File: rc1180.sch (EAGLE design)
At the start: 10 parts, among them IC1 LD117AS33TR

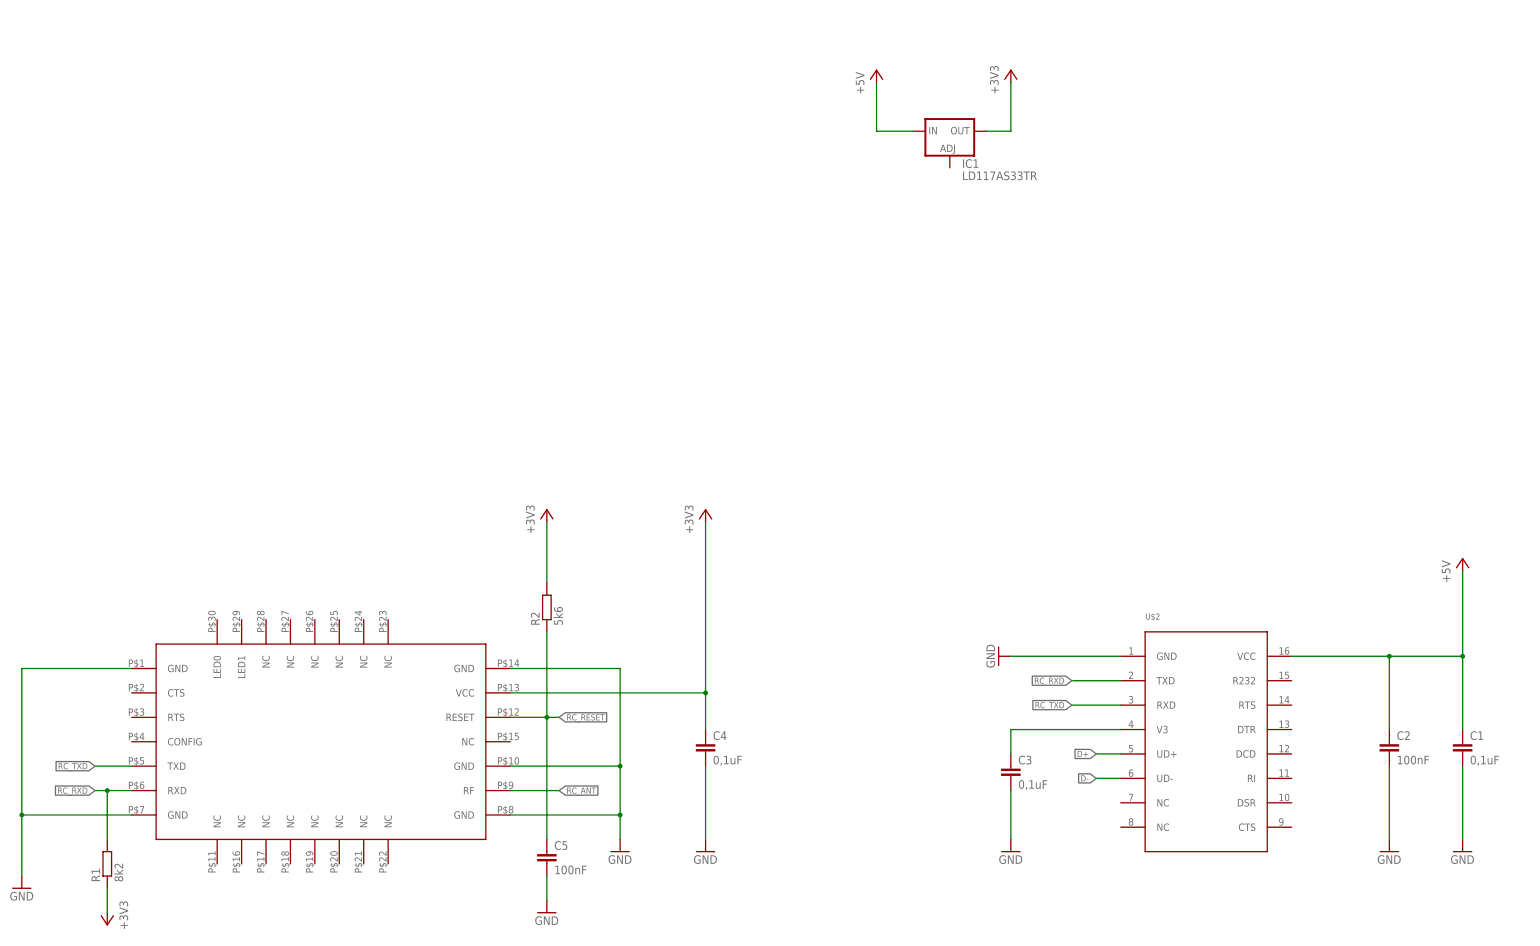
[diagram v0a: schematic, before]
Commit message: Added ch340 and ams1117 vreg
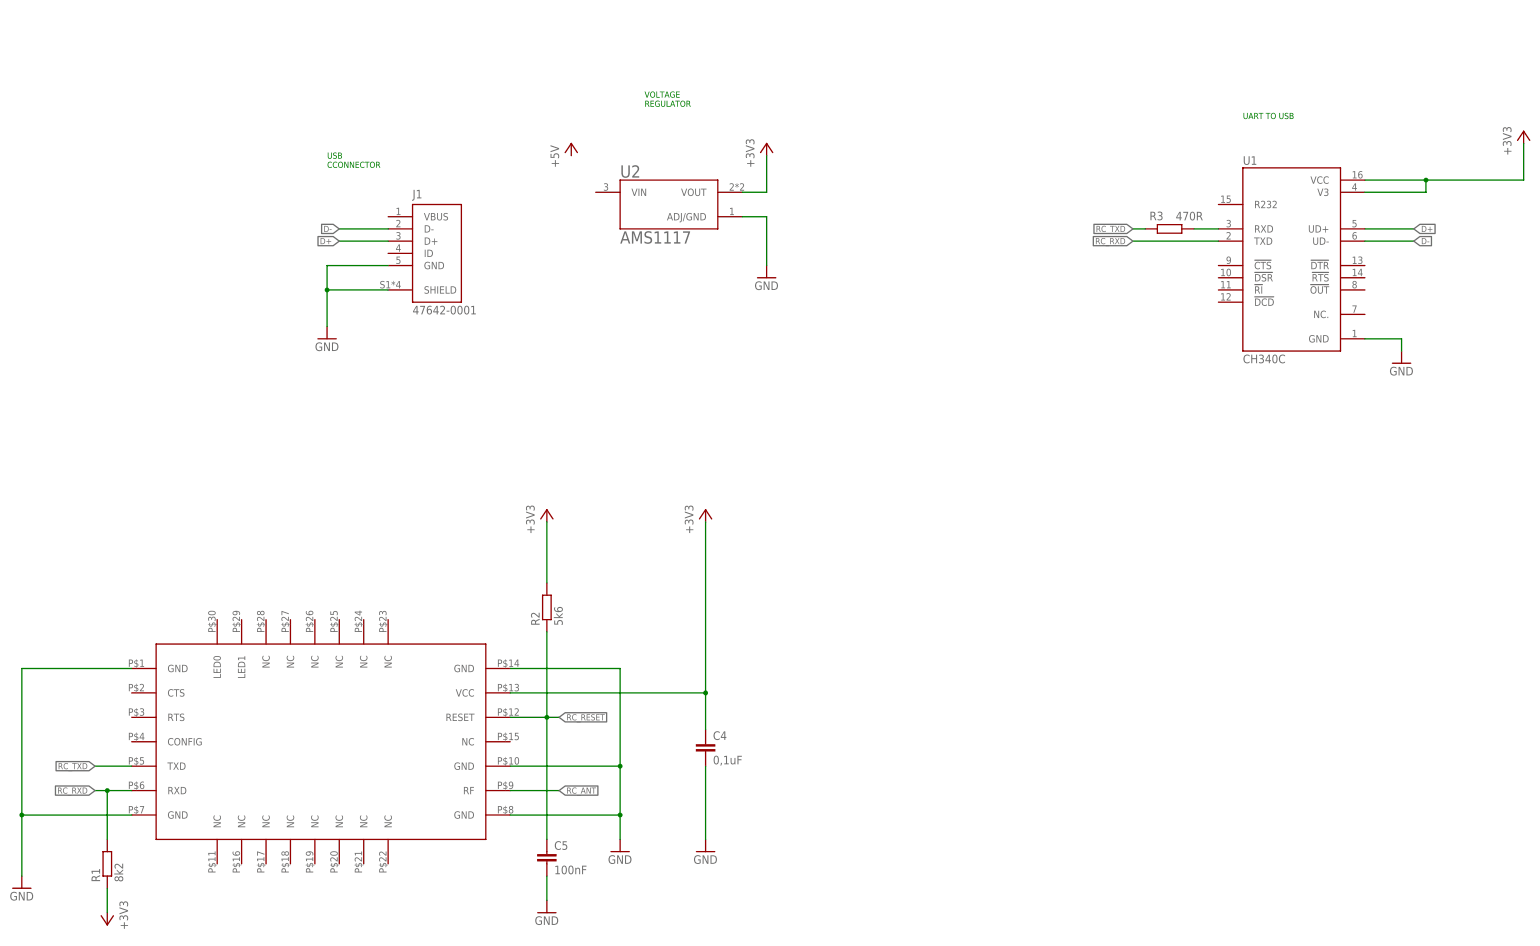
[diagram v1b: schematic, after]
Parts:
- removed C1, C3: 0,1uF, rcl:C-EUC1206K
- removed C2: 100nF, rcl:C-EUC0805
- removed IC1: LD117AS33TR, v-reg:LD117AS33TR
- removed U$2: CH340C, jacek27:CH340C
- added J1: 47642-0001, 47642-0001:47642-0001
- added R3: 470R, rcl:R-EU_R0805
- added U1: CH340C, CH340C:CH340C
- added U2: AMS1117, AMS1117:AMS1117
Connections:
- removed net +5V: C1.1, C2.1, IC1.IN, U$2.VCC
- net +3V3: now also U1.V3, U1.VCC, U2.VOUT; no longer IC1.OUT
- net D+: now also J1.D+, U1.UD+; no longer U$2.UD+
- net D-: now also J1.D-, U1.UD-; no longer U$2.UD-
- net GND: now also J1.GND, J1.SHIELD, U1.GND, U2.ADJ/GND; no longer C1.2, C2.2, C3.2, U$2.GND
- net N$1: now also R3.2, U1.RXD; no longer C3.1, U$2.V3
- net RC_RXD: now also U1.TXD; no longer U$2.TXD
- net RC_TXD: now also R3.1; no longer U$2.RXD
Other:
- note added: "UART TO USB"
- note added: "USB CCONNECTOR"
- note added: "VOLTAGE REGULATOR"

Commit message: Component placed / frame added
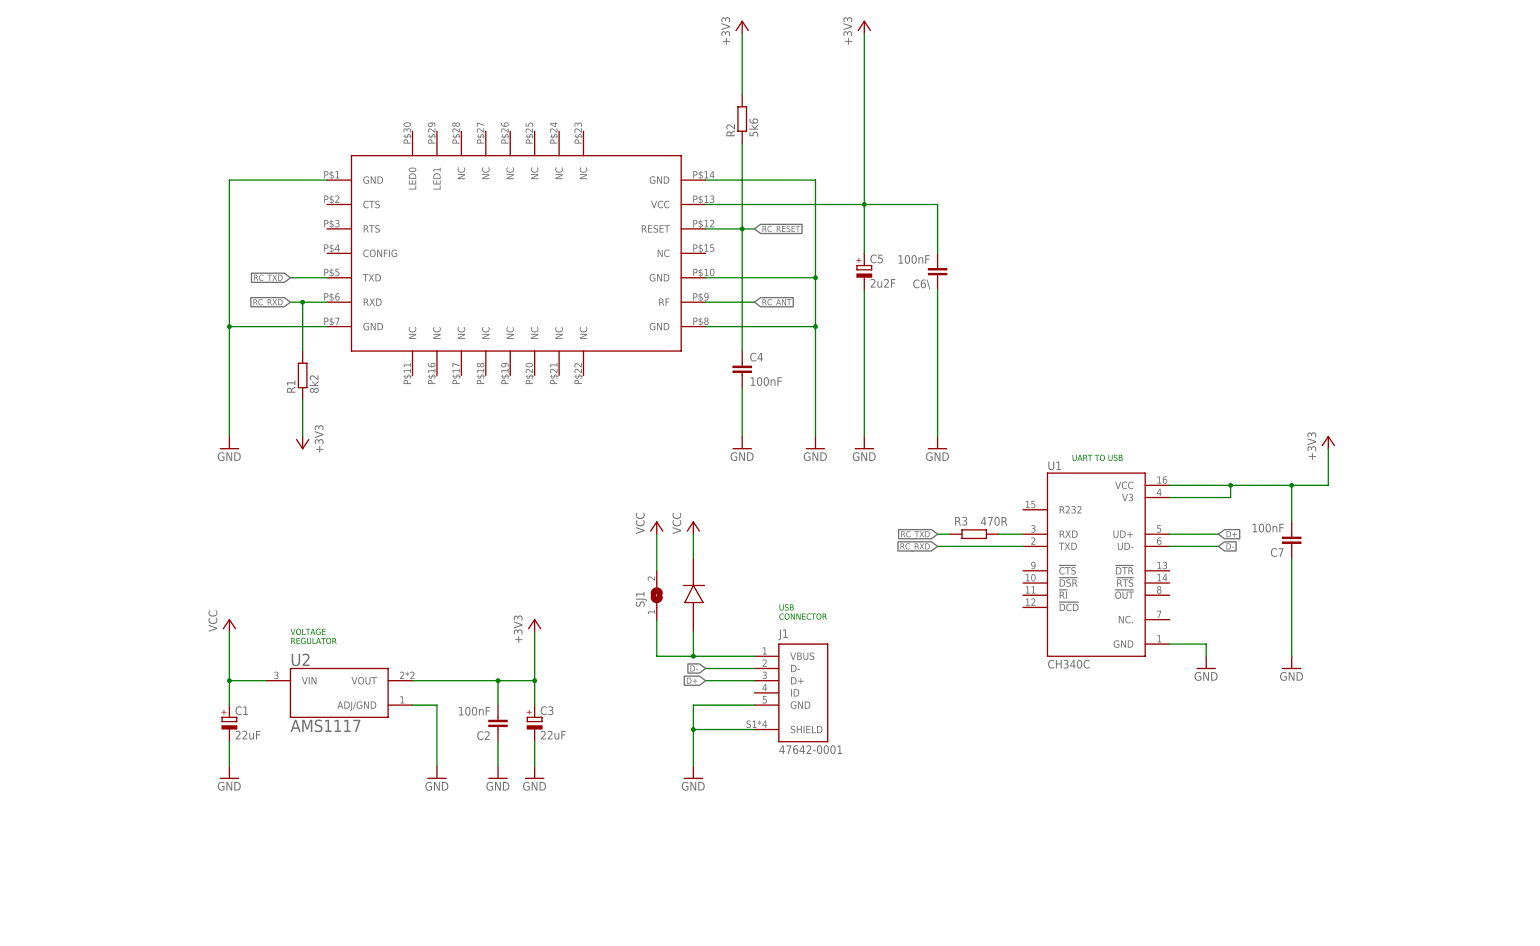
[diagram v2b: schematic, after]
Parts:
- added C1, C3: 22uF, rcl:CPOL-EUC/6032-28R
- added C2, C6\, C7: 100nF, rcl:C-EUC0805K
- added SJ1: (no value), jumper:SJ
- added U$2: MBR0540, MBR0540:MBR0540
- C4: value 0,1uF -> 100nF; device rcl:C-EUC1206K -> rcl:C-EUC0805
- C5: value 100nF -> 2u2F; device rcl:C-EUC0805 -> rcl:CPOL-EUA/3216-18W; TME_PN (none) -> T491A225K020AT
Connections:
- new net N$2: J1.VBUS, SJ1.1, U$2.A
- new net VCC: C1.+, SJ1.2, U$2.K, U2.VIN
- net +3V3: now also C2.2, C3.+, C5.+, C6\.2, C7.2; no longer C4.1
- net GND: now also C1.-, C2.1, C3.-, C5.-, C6\.1, C7.1; no longer C5.2
- net RC_RESET: now also C4.1; no longer C5.1
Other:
- note added: "USB CONNECTOR"
- note removed: "USB CCONNECTOR"
- moved on the sheet: C4, J1, R1, R2, R3, U1, U2

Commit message: Final touches
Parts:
- removed C2: 100nF, rcl:C-EUC0805K
- added X1: SMA-142-0701-801/806, con-coax:SMA-142-0701-801/806
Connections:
- net +3V3: no longer C2.2
- net GND: now also X1.2; no longer C2.1
- net RC_ANT: now also X1.1
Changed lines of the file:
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@@
 <part name="+3V5" library="supply1" library_urn="urn:adsk.eagle:library:371" deviceset="+3V3" device=""/>
 <part name="C7" library="rcl" library_urn="urn:adsk.eagle:library:334" deviceset="C-EU" device="C0805K" package3d_urn="urn:adsk.eagle:package:23681/2" value="100nF"/>
-<part name="C2" library="rcl" library_urn="urn:adsk.eagle:library:334" deviceset="C-EU" device="C0805K" package3d_urn="urn:adsk.eagle:package:23681/2" value="100nF"/>
 <part name="C6\" library="rcl" library_urn="urn:adsk.eagle:library:334" deviceset="C-EU" device="C0805K" package3d_urn="urn:adsk.eagle:package:23681/2" value="100nF"/>
 <part name="GND4" library="supply1" library_urn="urn:adsk.eagle:library:371" deviceset="GND" device=""/>
@@
 <attribute name="TME_PN" value="293D226X9010C2TE3"/>
 </part>
-<part name="GND6" library="supply1" library_urn="urn:adsk.eagle:library:371" deviceset="GND" device=""/>
 <part name="GND11" library="supply1" library_urn="urn:adsk.eagle:library:371" deviceset="GND" device=""/>
 <part name="GND12" library="supply1" library_urn="urn:adsk.eagle:library:371" deviceset="GND" device=""/>
@@
 <part name="P+3" library="supply1" library_urn="urn:adsk.eagle:library:371" deviceset="VCC" device=""/>
 <part name="FRAME1" library="frames" library_urn="urn:adsk.eagle:library:229" deviceset="A4L-LOC" device=""/>
+<part name="X1" library="con-coax" library_urn="urn:adsk.eagle:library:133" deviceset="SMA-" device="142-0701-801/806" package3d_urn="urn:adsk.eagle:package:6214/1"/>
+<part name="GND13" library="supply1" library_urn="urn:adsk.eagle:library:371" deviceset="GND" device=""/>
 </parts>
 <sheets>
@@
 <attribute name="VALUE" x="234.696" y="65.659" size="1.778" layer="96" rot="R180"/>
 </instance>
-<instance part="C2" gate="G$1" x="71.12" y="22.86" smashed="yes" rot="R180">
-<attribute name="NAME" x="69.596" y="22.479" size="1.778" layer="95" rot="R180"/>
-<attribute name="VALUE" x="69.596" y="27.559" size="1.778" layer="96" rot="R180"/>
-</instance>
 <instance part="C6\" gate="G$1" x="162.56" y="116.84" smashed="yes" rot="R180">
 <attribute name="NAME" x="161.036" y="116.459" size="1.778" layer="95" rot="R180"/>
@@
 <attribute name="TME_PN" x="78.74" y="25.4" size="1.27" layer="96" display="off"/>
 </instance>
-<instance part="GND6" gate="1" x="71.12" y="12.7" smashed="yes">
-<attribute name="VALUE" x="68.58" y="10.16" size="1.778" layer="96"/>
-</instance>
 <instance part="GND11" gate="1" x="78.74" y="12.7" smashed="yes">
 <attribute name="VALUE" x="76.2" y="10.16" size="1.778" layer="96"/>
@@
 <attribute name="LAST_DATE_TIME" x="217.17" y="10.16" size="2.286" layer="94"/>
 <attribute name="SHEET" x="230.505" y="5.08" size="2.54" layer="94"/>
+</instance>
+<instance part="X1" gate="G1" x="215.9" y="139.7" smashed="yes" rot="R180">
+<attribute name="VALUE" x="218.44" y="144.78" size="1.778" layer="96" rot="R180"/>
+<attribute name="NAME" x="218.44" y="136.398" size="1.778" layer="95" rot="R180"/>
+</instance>
+<instance part="GND13" gate="1" x="187.96" y="129.54" smashed="yes">
+<attribute name="VALUE" x="185.42" y="127" size="1.778" layer="96"/>
 </instance>
 </instances>
@@
 </segment>
 <segment>
-<pinref part="C2" gate="G$1" pin="1"/>
-<pinref part="GND6" gate="1" pin="GND"/>
-<wire x1="71.12" y1="20.32" x2="71.12" y2="15.24" width="0.1524" layer="91"/>
-</segment>
-<segment>
 <pinref part="C3" gate="G$1" pin="-"/>
 <pinref part="GND11" gate="1" pin="GND"/>
 <wire x1="78.74" y1="20.32" x2="78.74" y2="15.24" width="0.1524" layer="91"/>
+</segment>
+<segment>
+<pinref part="X1" gate="G1" pin="2"/>
+<wire x1="213.36" y1="142.24" x2="187.96" y2="142.24" width="0.1524" layer="91"/>
+<pinref part="GND13" gate="1" pin="GND"/>
+<wire x1="187.96" y1="142.24" x2="187.96" y2="132.08" width="0.1524" layer="91"/>
 </segment>
 </net>
@@
 <segment>
 <pinref part="U2" gate="G$1" pin="VOUT"/>
-<wire x1="53.34" y1="33.02" x2="71.12" y2="33.02" width="0.1524" layer="91"/>
+<wire x1="53.34" y1="33.02" x2="78.74" y2="33.02" width="0.1524" layer="91"/>
 <pinref part="C3" gate="G$1" pin="+"/>
-<wire x1="71.12" y1="33.02" x2="78.74" y2="33.02" width="0.1524" layer="91"/>
 <wire x1="78.74" y1="33.02" x2="78.74" y2="27.94" width="0.1524" layer="91"/>
-<pinref part="C2" gate="G$1" pin="2"/>
-<wire x1="71.12" y1="27.94" x2="71.12" y2="33.02" width="0.1524" layer="91"/>
-<junction x="71.12" y="33.02"/>
 <pinref part="+3V3" gate="G$1" pin="+3V3"/>
 <wire x1="78.74" y1="43.18" x2="78.74" y2="33.02" width="0.1524" layer="91"/>
@@
 <label x="124.46" y="111.76" size="1.27" layer="95" xref="yes"/>
 </segment>
-</net>
+<segment>
+<pinref part="X1" gate="G1" pin="1"/>
+<wire x1="213.36" y1="139.7" x2="203.2" y2="139.7" width="0.1524" layer="91"/>
+<label x="203.2" y="139.7" size="1.27" layer="95" rot="R180" xref="yes"/>
+</segment>
+</net>

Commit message: Added holes and vias
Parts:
- added H1, H2, H3: MOUNT-HOLE2.8, holes:MOUNT-HOLE2.8
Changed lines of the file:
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@@
 <part name="X1" library="con-coax" library_urn="urn:adsk.eagle:library:133" deviceset="SMA-" device="142-0701-801/806" package3d_urn="urn:adsk.eagle:package:6214/1"/>
 <part name="GND13" library="supply1" library_urn="urn:adsk.eagle:library:371" deviceset="GND" device=""/>
+<part name="H1" library="holes" library_urn="urn:adsk.eagle:library:237" deviceset="MOUNT-HOLE" device="2.8" package3d_urn="urn:adsk.eagle:package:14271/1"/>
+<part name="H2" library="holes" library_urn="urn:adsk.eagle:library:237" deviceset="MOUNT-HOLE" device="2.8" package3d_urn="urn:adsk.eagle:package:14271/1"/>
+<part name="H3" library="holes" library_urn="urn:adsk.eagle:library:237" deviceset="MOUNT-HOLE" device="2.8" package3d_urn="urn:adsk.eagle:package:14271/1"/>
 </parts>
 <sheets>
@@
 <attribute name="VALUE" x="185.42" y="127" size="1.778" layer="96"/>
 </instance>
+<instance part="H1" gate="G$1" x="218.44" y="127" smashed="yes">
+<attribute name="NAME" x="220.472" y="127.5842" size="1.778" layer="95"/>
+<attribute name="VALUE" x="220.472" y="124.5362" size="1.778" layer="96"/>
+</instance>
+<instance part="H2" gate="G$1" x="218.44" y="119.38" smashed="yes">
+<attribute name="NAME" x="220.472" y="119.9642" size="1.778" layer="95"/>
+<attribute name="VALUE" x="220.472" y="116.9162" size="1.778" layer="96"/>
+</instance>
+<instance part="H3" gate="G$1" x="218.44" y="111.76" smashed="yes">
+<attribute name="NAME" x="220.472" y="112.3442" size="1.778" layer="95"/>
+<attribute name="VALUE" x="220.472" y="109.2962" size="1.778" layer="96"/>
+</instance>
 </instances>
